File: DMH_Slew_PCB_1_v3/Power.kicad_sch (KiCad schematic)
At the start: 29 parts, among them J0 Conn_01x01, J100 IDC_02x08, J200 IDC_02x05, J50 Conn_01x08_PinHeader, J51 Conn_01x08_PinHeader, J60 Conn_01x08_PinHeader, J61 Conn_01x08_PinHeader, U1 TL074, U10 LM4040LP-10, U11 LM4040LP-10, U2 TL074, U3 TL074, U4 TL074

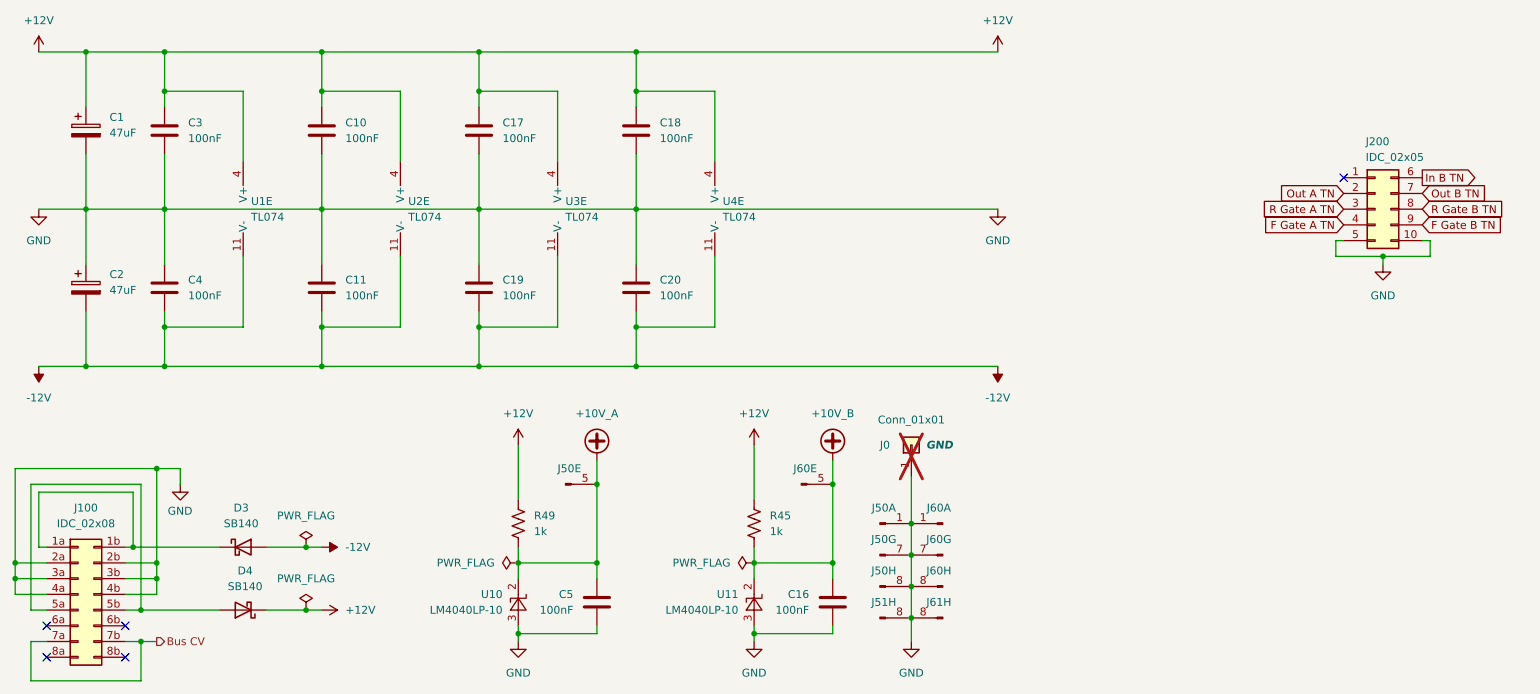
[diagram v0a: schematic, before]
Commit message: V3 sch redesign ongoing
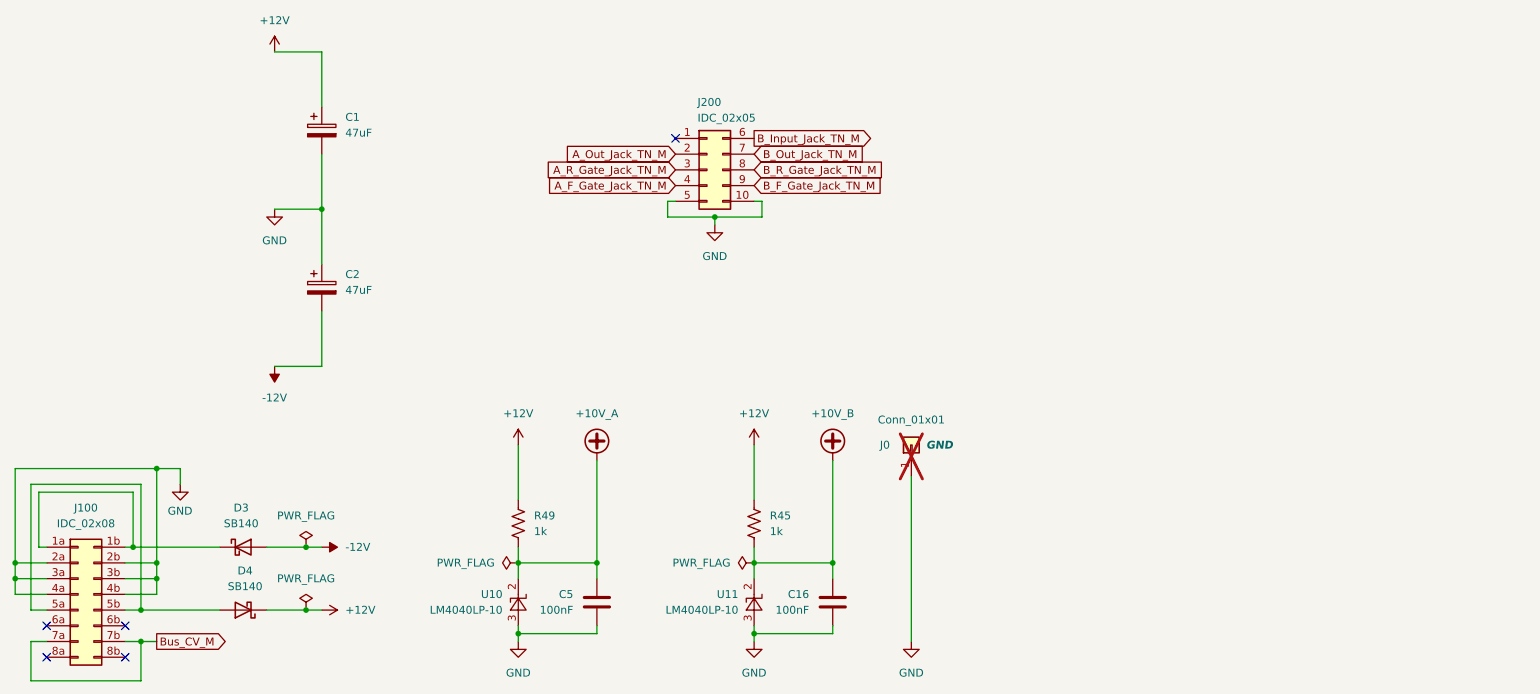
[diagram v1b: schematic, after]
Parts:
- removed C10, C11, C17, C18, C19, C20, C3, C4: 100nF, Capacitor_THT:C_Disc_D4.3mm_W1.9mm_P5.00mm, symbol Device:C
- removed J50, J51, J60, J61: Conn_01x08_PinHeader, Connector_PinHeader_2.54mm:PinHeader_1x08_P2.54mm_Vertical, symbol SynthStuff:Conn_01x08_PinHeader
- removed U1, U2, U3, U4: TL074, Package_DIP:DIP-14_W7.62mm_Socket, symbol Amplifier_Operational:TL074
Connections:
- net Bus CV renamed Bus_CV_M
- net F Gate A TN renamed A_F_Gate_Jack_TN_M
- net F Gate B TN renamed B_F_Gate_Jack_TN_M
- net In B TN renamed B_Input_Jack_TN_M
- net Out A TN renamed A_Out_Jack_TN_M
- net Out B TN renamed B_Out_Jack_TN_M
- net R Gate A TN renamed A_R_Gate_Jack_TN_M
- net R Gate B TN renamed B_R_Gate_Jack_TN_M
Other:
- moved on the sheet: C1, C2, J200
